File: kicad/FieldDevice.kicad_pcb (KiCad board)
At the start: 2 copper layers, 53.5 x 38.5 mm, 36 parts, among them P201 Positive, P202 Negative, P301 CONN_01X06, SW301 SW_PUSH, U101 DS7505

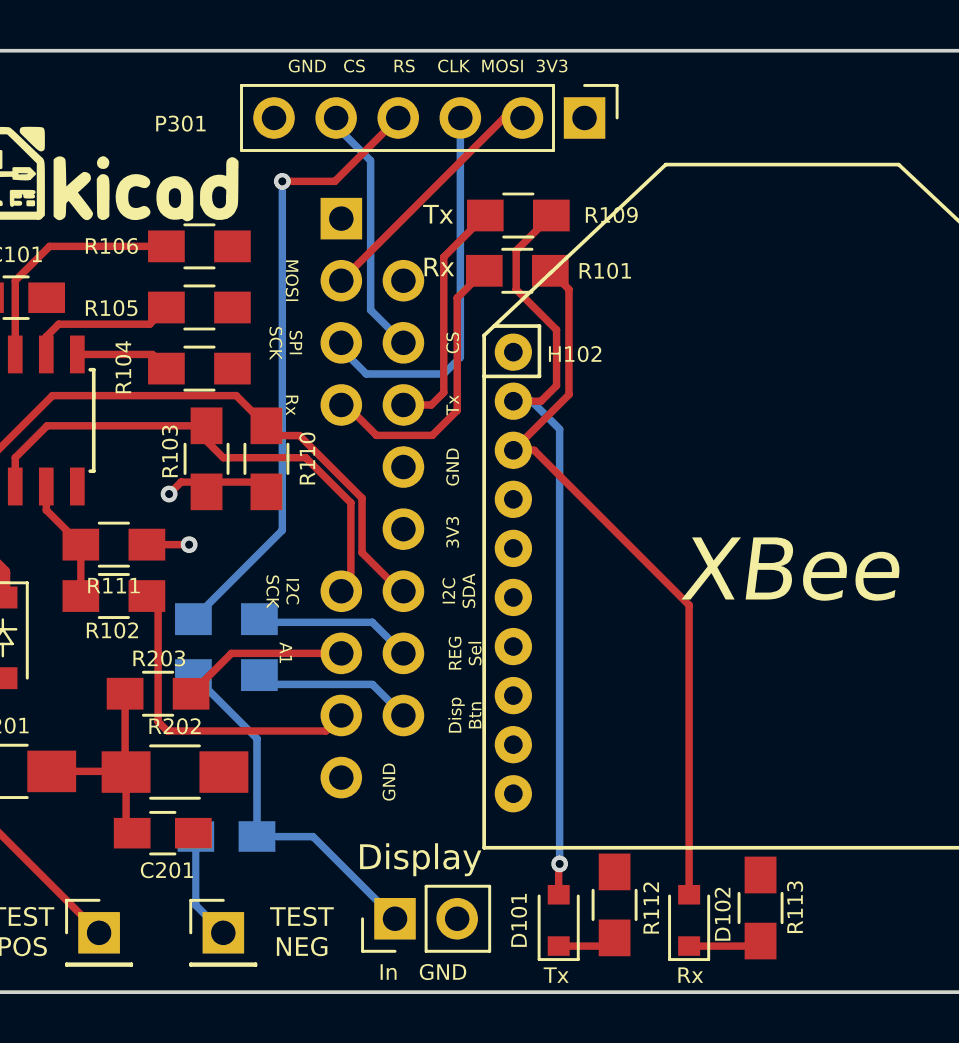
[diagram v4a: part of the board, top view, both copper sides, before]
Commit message: Altered the display connector for the DOG104 i.e. general purpose
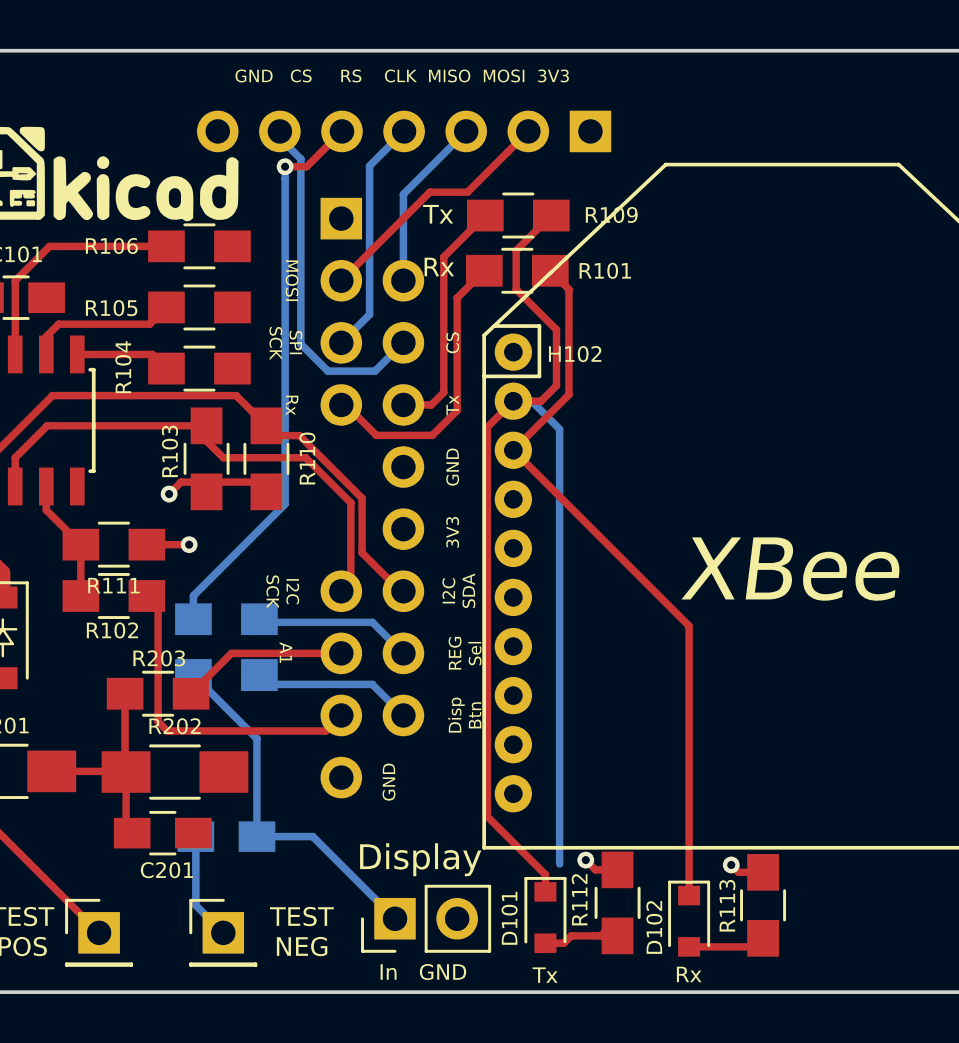
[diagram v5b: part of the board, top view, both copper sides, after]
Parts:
- D101: value LED -> Tx
- D102: value LED -> Rx
- P301: value CONN_01X06 -> Conn_01x07_Female; footprint Pin_Headers:Pin_Header_Straight_1x06_Pitch2.54mm -> Pin_Headers:Pin_Header_Angled_1x07_Pitch2.54mm; moved to B.Cu
- R202: value 30kΩ 125mW 0.1% -> 270kΩ 125mW 0.1%
- moved P301 0.60 mm to (140.5, 67.3), turned to 90 degrees
- moved D101 0.55 mm to (138.7, 99.5), turned to 270 degrees
- moved R113 0.15 mm to (147.6, 99.0), turned to 90 degrees
- moved R112 0.15 mm to (141.6, 98.8), turned to 90 degrees
- turned D102 to 270 degrees
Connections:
- net /Analog_Sensors/ANLG_1 renamed /ANLG_1
- net /Display/Display renamed /Display
- net /Display/MOSI renamed /MOSI
- C101 pad 1: /Display/3V3 -> /3V3
- D101 pad 1: Net-(D101-Pad1) -> /TX
- D101 pad 2: /TX -> Net-(D101-Pad2)
- D102 pad 1: Net-(D102-Pad1) -> /RX
- D102 pad 2: /RX -> Net-(D102-Pad2)
- H101 pad 12: /Display/3V3 -> /3V3
- H101 pad 4: (no net) -> /MISO
- H101 pad 5: /Display/SPI_SCK -> /SPI_CLK
- H101 pad 6: /Display/CS -> /CS
- H102 pad 1: /Display/3V3 -> /3V3
- P301 pad 1: /Display/3V3 -> /3V3
- P301 pad 3: /Display/SPI_SCK -> /MISO
- P301 pad 4: /Display/RS -> /SPI_CLK
- P301 pad 5: /Display/CS -> /REG_SEL
- P301 pad 6: GND -> /CS
- R103 pad 2: /Display/3V3 -> /3V3
- R107 pad 1: /Display/RS -> /REG_SEL
- R110 pad 2: /Display/3V3 -> /3V3
- R111 pad 1: /Display/3V3 -> /3V3
- R112 pad 1: GND -> Net-(D101-Pad2)
- R112 pad 2: Net-(D101-Pad1) -> /3V3
- R113 pad 1: GND -> Net-(D102-Pad2)
- R113 pad 2: Net-(D102-Pad1) -> /3V3
- U101 pad 8: /Display/3V3 -> /3V3
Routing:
- net /Display/RS: track 25.4 -> 0.00 mm, vias 1 -> 0
- net /REG_SEL: track 0.00 -> 23.3 mm, vias 0 -> 1
- net /TX: track 32.7 -> 52.9 mm, vias 1 -> 0
- net /Display/SPI_SCK: track 15.6 -> 0.00 mm
- net /CS: track 0.00 -> 14.2 mm
- net /3V3: track 0.00 -> 14.1 mm, vias 0 -> 5
- net /Display/3V3: track 11.2 -> 0.00 mm, vias 3 -> 0
- net /Display/CS: track 10.3 -> 0.00 mm
- net /SPI_CLK: track 0.00 -> 10.1 mm
- net /MISO: track 0.00 -> 7.17 mm
- net Net-(D101-Pad2): track 0.00 -> 3.35 mm
- net Net-(D102-Pad2): track 0.00 -> 3.17 mm
- net Net-(D102-Pad1): track 3.01 -> 0.00 mm
- net Net-(D101-Pad1): track 2.42 -> 0.00 mm
- added copper zone on B.Cu, net /3V3
- removed copper zone on B.Cu, net /Display/3V3
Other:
- board text added: "GND CS RS CLK MISO MOSI 3V3"
- board text removed: "GND CS RS CLK MOSI 3V3"

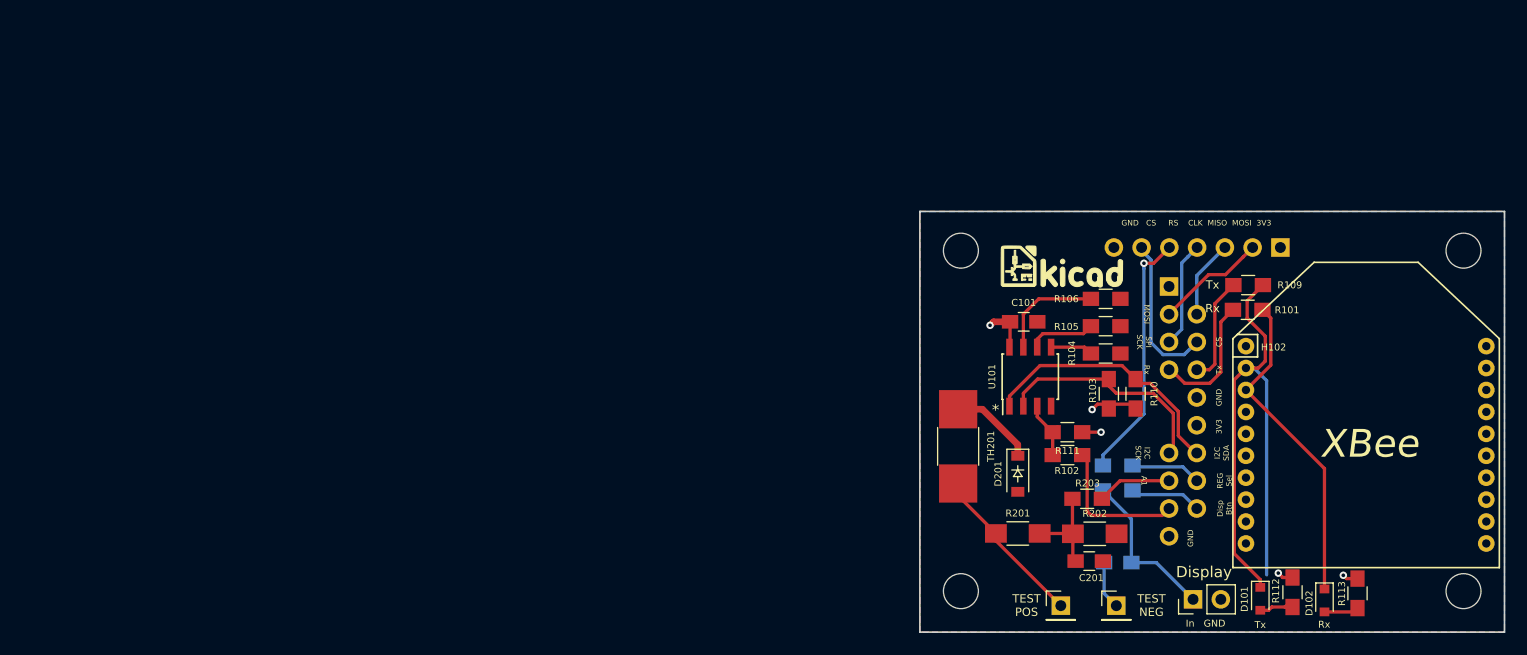
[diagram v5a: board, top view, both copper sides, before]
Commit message: Completed the new schematic (draft) and started the layout to verify the design
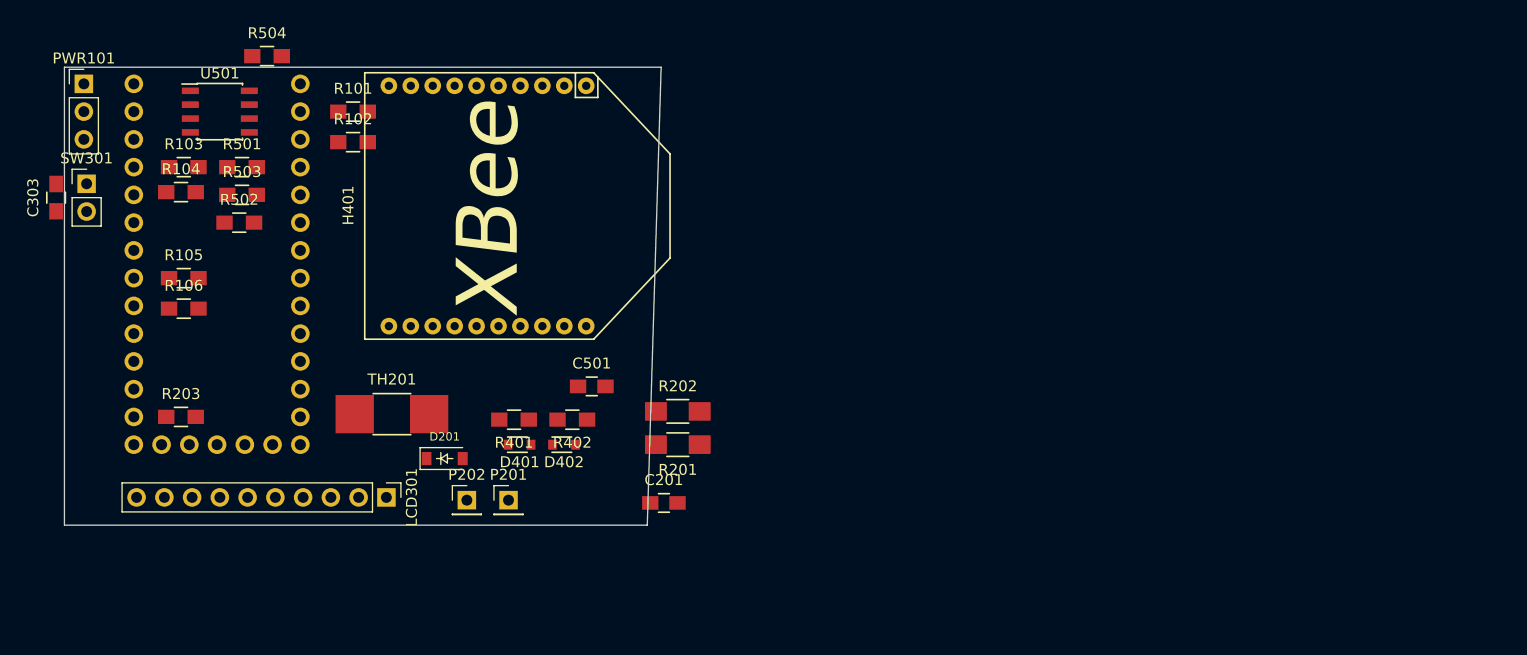
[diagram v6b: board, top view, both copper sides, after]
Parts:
- removed C101: 100pF 50V, Capacitors_SMD:C_0805_HandSoldering
- removed D101: Tx, Diodes_SMD:D_0805
- removed D102: Rx, Diodes_SMD:D_0805
- removed G***: LOGO, FieldDevice_Footprints:MyBasic_rounded_50_1
- removed G***: LOGO, FieldDevice_Footprints:KiCad-Logo
- removed H101: CE_Socket, CE_Header:CE_Socket
- removed H102: DIGI_XBEE, FieldDevice_Footprints:XBEE_S2C
- removed P301: Conn_01x07_Female, Pin_Headers:Pin_Header_Angled_1x07_Pitch2.54mm
- removed R107, R108: 0Ω, Resistors_SMD:R_0805_HandSoldering
- removed R109: 0, Resistors_SMD:R_0805_HandSoldering
- removed R110: 4k7Ω, Resistors_SMD:R_0805_HandSoldering
- removed R111: 10k, Resistors_SMD:R_0805_HandSoldering
- removed R112, R113: 680Ω, Resistors_SMD:R_0805_HandSoldering
- removed REF** (x4): MountingHole_3.2mm_M3, Mounting_Holes:MountingHole_3.2mm_M3
- added C501: 100pF 50V, Capacitors_SMD:C_0805_HandSoldering, F.Cu at (77.5, 80.0)
- added D401: Tx, Diodes_SMD:D_0805, F.Cu at (70.9, 85.3)
- added D402: Rx, Diodes_SMD:D_0805, F.Cu at (74.9, 85.3)
- added H401: DIGI_XBEE, FieldDevice_Footprints:XBEE_S2C, F.Cu at (77.0, 63.5)
- added LCD301: EA_DISPLAY, Pin_Headers:Pin_Header_Straight_1x10_Pitch2.54mm, F.Cu at (58.7, 90.2)
- added PWR101: FD_POWER, Pin_Headers:Pin_Header_Straight_1x03_Pitch2.54mm, F.Cu at (31.0, 52.3)
- added R401: 680Ω, Resistors_SMD:R_0805_HandSoldering, F.Cu at (70.4, 83.1)
- added R402: 680Ω, Resistors_SMD:R_0805_HandSoldering, F.Cu at (75.7, 83.1)
- added R501: 10k, Resistors_SMD:R_0805_HandSoldering, F.Cu at (45.5, 59.9)
- added R502: 0, Resistors_SMD:R_0805_HandSoldering, F.Cu at (45.2, 65.0)
- added R503: 0, Resistors_SMD:R_0805_HandSoldering, F.Cu at (45.5, 62.5)
- added R504: 0, Resistors_SMD:R_0805_HandSoldering, F.Cu at (47.8, 49.8)
- added U501: DS7505, Housings_SOIC:SOIC-8_3.9x4.9mm_Pitch1.27mm, F.Cu at (43.4, 54.9)
- C303: moved to F.Cu
- R103: value 4k7Ω -> 0Ω
- R104: value 0 -> 0Ω
- R105, R106: value 0 -> 4k7Ω
- U101: value DS7505 -> Teensy-3.2; footprint Housings_SOIC:SOIC-8_3.9x4.9mm_Pitch1.27mm -> FieldDevice_Footprints:Teensy-32; moved to B.Cu
- moved SW301 108.2 mm to (31.2, 61.5), turned to 0 degrees
- moved C303 102.7 mm to (28.4, 62.7), turned to 90 degrees
- moved R103 87.2 mm to (40.1, 59.9), turned to 0 degrees
- moved R104 85.9 mm to (39.9, 62.2)
- moved R105 84.5 mm to (40.1, 70.1)
- moved R106 84.4 mm to (40.1, 72.9)
- moved R101 83.9 mm to (55.6, 54.9)
- moved R203 83.3 mm to (39.9, 82.8)
- moved U101 75.3 mm to (43.2, 67.6), turned to 180 degrees
- moved R102 71.4 mm to (55.6, 57.7), turned to 0 degrees
- moved P202 60.2 mm to (66.0, 90.4)
- moved D201 52.5 mm to (64.0, 86.6), turned to 0 degrees
- moved TH201 51.9 mm to (59.2, 82.5), turned to 0 degrees
- moved P201 51.5 mm to (69.8, 90.4)
- moved R202 39.8 mm to (85.3, 82.3)
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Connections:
- R101 pad 1: Net-(H101-Pad7) -> /Rx
- R101 pad 2: /RX -> Net-(R101-Pad2)
- R102 pad 1: Net-(H101-Pad17) -> /TX
- R102 pad 2: /OverTemp -> Net-(R102-Pad2)
- R103 pad 1: /I2C_SCK -> Net-(R103-Pad1)
- R103 pad 2: /3V3 -> /OverTemp
- R104 pad 2: GND -> /Display
- R105 pad 1: Net-(R105-Pad1) -> /3V3
- R105 pad 2: GND -> /I2C_SCK
- R106 pad 1: Net-(R106-Pad1) -> /3V3
- R106 pad 2: GND -> /I2C_SDA
- U101 pad 1: /SDA -> Net-(R102-Pad2)
- U101 pad 2: /I2C_SCK -> (no net)
- U101 pad 3: /OverTemp -> (no net)
- U101 pad 4: GND -> (no net)
- U101 pad 5: Net-(R104-Pad1) -> (no net)
- U101 pad 6: Net-(R105-Pad1) -> (no net)
- U101 pad 7: Net-(R106-Pad1) -> (no net)
- U101 pad 8: /3V3 -> (no net)
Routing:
- net /TX: track 52.9 -> 0.00 mm
- net /RX: track 29.8 -> 0.00 mm
- net /SDA: track 24.0 -> 0.00 mm
- net /REG_SEL: track 23.3 -> 0.00 mm, vias 1 -> 0
- net /I2C_SCK: track 21.7 -> 0.00 mm
- net /Analog_Sensors/TEST_POS_1: track 15.2 -> 0.00 mm
- net /Display: track 14.7 -> 0.00 mm
- net /CS: track 14.2 -> 0.00 mm
- net /3V3: track 14.1 -> 0.00 mm, vias 5 -> 0
- net Net-(H101-Pad17): track 13.5 -> 0.00 mm
- net Net-(H101-Pad7): track 12.2 -> 0.00 mm
- net Net-(R106-Pad1): track 10.6 -> 0.00 mm
- net /MOSI: track 10.2 -> 0.00 mm
- net /SPI_CLK: track 10.1 -> 0.00 mm
- net Net-(H101-Pad8): track 9.80 -> 0.00 mm
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- removed copper zone on B.Cu, net /3V3
- removed copper zone on F.Cu, net GND
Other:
- board size 53.5 x 38.5 mm -> 54.6 x 41.9 mm
- net class Default: clearance 0.1524 -> 0.2; trace_width 0.1524 -> 0.25; via_dia 0.6858 -> 0.6; via_drill 0.3302 -> 0.4
- rule trace_clearance: 0.1524 -> 0.2
- rule trace_min: 0.1524 -> 0.2
- rule via_min_drill: 0.3302 -> 0.3
- rule via_min_size: 0.6858 -> 0.4
- board text removed: "*"
- board text removed: "3V3"
- board text removed: "A1"
- board text removed: "CS"
- board text removed: "Disp Btn"
- board text removed: "Display"
- board text removed: "GND"
- board text removed: "GND CS RS CLK MISO MOSI 3V3"
- board text removed: "I2C SCK"
- board text removed: "I2C SDA"
- board text removed: "In GND"
- board text removed: "Leawood Field Device Voltage Sensor 2L_3"
- board text removed: "MOSI"
- board text removed: "PWR"
- board text removed: "REG Sel"
- board text removed: "Rx"
- board text removed: "SPI SCK"
- board text removed: "TEST NEG"
- board text removed: "TEST POS"
- board text removed: "Tx"

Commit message: Completed the draft of REV2
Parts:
- added Q301: Q_PMOS_GSD, TO_SOT_Packages_SMD:SOT-23, F.Cu at (32.0, 82.8)
- added ST**: STITCH_VIA, FieldDevice_Footprints:STITCH_VIA, F.Cu at (71.9, 56.0)
- added ST**: STITCH_VIA, FieldDevice_Footprints:STITCH_VIA, F.Cu at (70.7, 53.7)
- added ST**: STITCH_VIA, FieldDevice_Footprints:STITCH_VIA, F.Cu at (70.7, 53.0)
- LCD301: footprint Pin_Headers:Pin_Header_Straight_1x10_Pitch2.54mm -> Pin_Headers:Pin_Header_Angled_1x10_Pitch2.54mm; moved to B.Cu
- U101: moved to F.Cu
- moved LCD301 27.8 mm to (31.0, 88.3)
- moved U501 23.1 mm to (62.5, 67.9)
- moved R202 22.9 mm to (63.0, 87.2), turned to 180 degrees
- moved R504 22.2 mm to (66.5, 61.7), turned to 90 degrees
- moved R503 19.1 mm to (64.5, 61.7), turned to 90 degrees
- moved R103 18.7 mm to (58.7, 62.5)
- moved C201 17.8 mm to (66.3, 89.9), turned to 180 degrees
- moved R502 17.6 mm to (62.5, 61.7), turned to 90 degrees
- moved C501 16.3 mm to (67.1, 67.4), turned to 270 degrees
- moved R101 16.2 mm to (71.8, 56.1), turned to 270 degrees
- moved R201 15.9 mm to (69.6, 87.2)
- moved R105 15.7 mm to (55.1, 65.5), turned to 270 degrees
- moved R106 15.1 mm to (55.0, 70.5), turned to 90 degrees
- moved R203 14.5 mm to (54.4, 83.3), turned to 180 degrees
- moved R102 14.2 mm to (69.7, 56.1), turned to 270 degrees
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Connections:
- net Net-(R502-Pad1) renamed /Temperature Sensor/A2
- net Net-(R503-Pad1) renamed /Temperature Sensor/A1
- net Net-(R504-Pad1) renamed /Temperature Sensor/A0
- LCD301 pad 1: (no net) -> Net-(LCD301-Pad1)
- LCD301 pad 10: (no net) -> GND
- LCD301 pad 8: (no net) -> /BACKLIGHT
- U101 pad 7: (no net) -> /BACKLIGHT
- U101 pad 8: (no net) -> /~DISP_ENABLE
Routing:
- net /3V3: track 0.00 -> 183.3 mm, vias 0 -> 6
- net Net-(R101-Pad2): track 0.00 -> 38.6 mm
- net Net-(R102-Pad2): track 0.00 -> 35.2 mm
- net /TX: track 0.00 -> 31.1 mm
- net /Rx: track 0.00 -> 27.4 mm
- net /BACKLIGHT: track 0.00 -> 26.5 mm
- net /5V: track 0.00 -> 20.8 mm
- net Net-(R104-Pad1): track 0.00 -> 19.0 mm
- net Net-(C201-Pad1): track 0.00 -> 16.8 mm
- net /Analog_Sensors/TEST_POS_1: track 0.00 -> 16.6 mm
- net /REG_SEL: track 0.00 -> 16.4 mm
- net /SPI_CLK: track 0.00 -> 14.7 mm
- net /I2C_SDA: track 0.00 -> 14.3 mm
- net /SPI_CS: track 0.00 -> 12.0 mm
- net /I2C_SCK: track 0.00 -> 11.0 mm
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- added copper zone on B.Cu, net GND
- added copper zone on F.Cu, net GND
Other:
- board size 54.6 x 41.9 mm -> 47 x 41.9 mm
- net class Default: clearance 0.2 -> 0.1524; trace_width 0.25 -> 0.1524; via_dia 0.6 -> 0.6858; via_drill 0.4 -> 0.3302
- rule pad_to_mask_clearance: 0 -> 0.0508
- rule trace_clearance: 0.2 -> 0.1524
- rule trace_min: 0.2 -> 0.1524
- rule via_min_drill: 0.3 -> 0.3302
- rule via_min_size: 0.4 -> 0.6858

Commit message: More changes to the layout for the Power System integration
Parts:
- added G***: LOGO, FieldDevice_Footprints:KiCad-Logo, B.Cu at (43.6, 75.4)
- added G***: LOGO, FieldDevice_Footprints:MyBasic_rounded_50_1, B.Cu at (43.3, 67.3)
- added G***: LOGO, FieldDevice_Footprints:MyBasic_rounded_50_1, F.Cu at (43.3, 67.3)
- added G***: LOGO, FieldDevice_Footprints:KiCad-Logo, F.Cu at (43.6, 75.4)
- added REF**: MountingHole_2.7mm_M2.5, Mounting_Holes:MountingHole_2.7mm_M2.5, F.Cu at (31.1, 77.0)
- added REF**: MountingHole_2.7mm_M2.5, Mounting_Holes:MountingHole_2.7mm_M2.5, F.Cu at (77.9, 48.9)
- added REF**: MountingHole_2.7mm_M2.5, Mounting_Holes:MountingHole_2.7mm_M2.5, F.Cu at (77.7, 90.8)
- added REF**: MountingHole_2.7mm_M2.5, Mounting_Holes:MountingHole_2.7mm_M2.5, F.Cu at (31.0, 48.8)
- C303, C501: footprint Capacitors_SMD:C_0805_HandSoldering -> Capacitors_SMD:C_0805
- PWR101: footprint Pin_Headers:Pin_Header_Straight_1x03_Pitch2.54mm -> Pin_Headers:Pin_Header_Angled_1x04_Pitch2.54mm; moved to B.Cu
- R101, R102, R103, R104, R105, R106, R203, R401, R402, R501, R502, R503, R504: footprint Resistors_SMD:R_0805_HandSoldering -> Resistors_SMD:R_0805
- R201, R202: footprint Resistors_SMD:R_1206_HandSoldering -> Resistors_SMD:R_1206
- moved PWR101 2.42 mm to (33.4, 52.2), turned to 180 degrees
- moved R203 2.41 mm to (56.8, 83.3)
- moved R104 2.09 mm to (32.3, 64.3)
- moved C303 2.09 mm to (32.3, 66.3)
- moved SW301 1.40 mm to (31.5, 70.1)
- moved U101 0.63 mm to (43.8, 67.6)
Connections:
- PWR101 pad 3: GND -> /BATT
- U101 pad 17: (no net) -> /BACKLIGHT
- U101 pad 2: (no net) -> /BATT
- U101 pad 7: /BACKLIGHT -> (no net)
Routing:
- net /3V3: track 183.3 -> 146.5 mm
- net /BACKLIGHT: track 26.5 -> 15.0 mm
- net /BATT: track 0.00 -> 3.90 mm
- net Net-(C201-Pad1): track 16.8 -> 14.4 mm
- net Net-(R101-Pad2): track 38.6 -> 36.7 mm
- net /5V: track 20.8 -> 19.0 mm
- net /ANLG_1: track 2.42 -> 4.19 mm
- net /SPI_CLK: track 14.7 -> 16.0 mm
- net /REG_SEL: track 16.4 -> 15.5 mm
- net /Display: track 7.00 -> 6.09 mm
- net /SPI_CS: track 12.0 -> 11.3 mm
- net Net-(R102-Pad2): track 35.2 -> 34.6 mm
- net /I2C_SDA: track 14.3 -> 13.7 mm
- net /I2C_SCK: track 11.0 -> 10.3 mm
- net /MISO: track 3.13 -> 3.69 mm
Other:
- board size 47 x 41.9 mm -> 50.4 x 45.7 mm
- board text added: "+5V"
- board text added: "3V3"
- board text added: "BATT"
- board text added: "BKL"
- board text added: "CLK"
- board text added: "CS"
- board text added: "GND"
- board text added: "Leawood Field Device Battery Monitor 2L_2"
- board text added: "MISO"
- board text added: "MOSI"
- board text added: "NC"
- board text added: "RS"
- board text added: "~EN"
- board text added: "~RST"
